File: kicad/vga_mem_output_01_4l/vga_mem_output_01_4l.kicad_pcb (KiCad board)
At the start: 4 copper layers, 80.4 x 110.6 mm, 61 parts, among them J1 Conn_01x03_Socket, J2 Conn_01x02_Socket, J3 Conn_01x08_Socket, J4 DE15_Socket_HighDensity_Mount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, J6 Conn_01x18_Socket, U1 74LS08, U10 74HCT574, U11 74HC245, U12 74AHC1GU04, U13 74LS163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

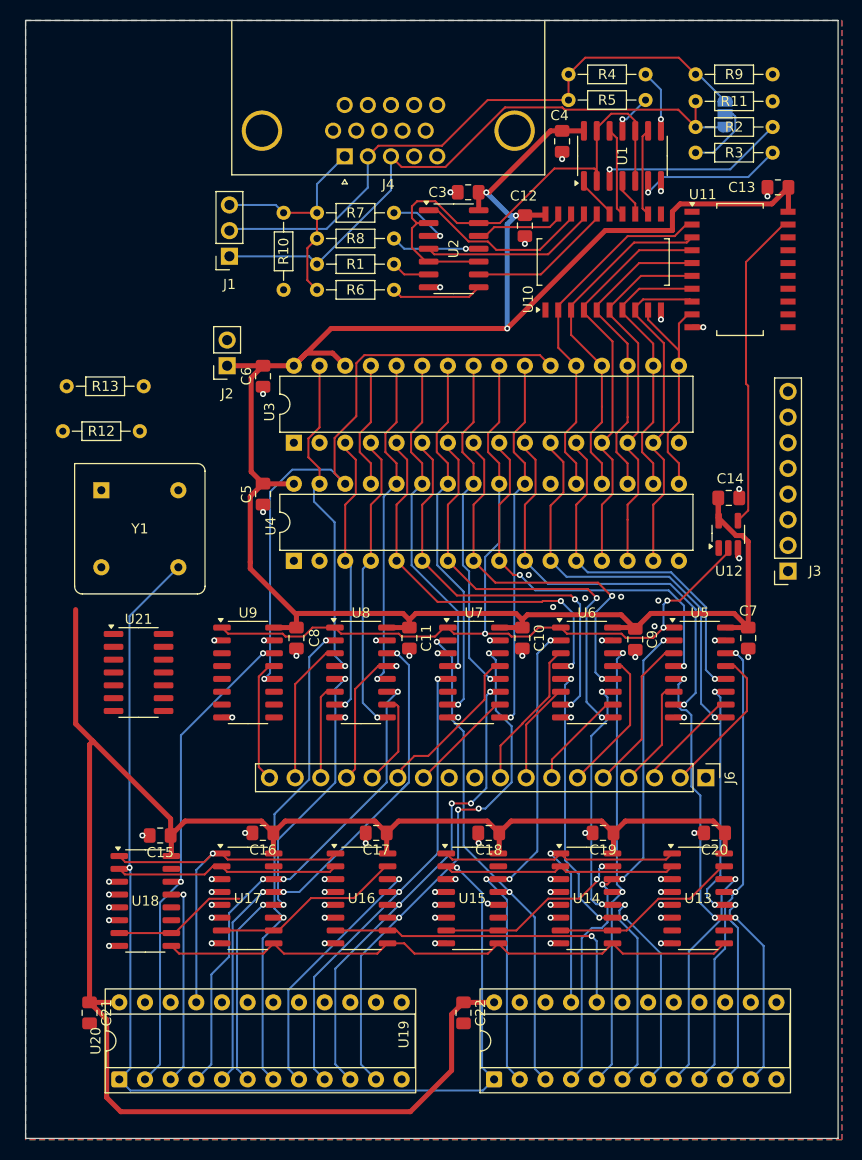
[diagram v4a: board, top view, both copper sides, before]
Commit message: finished vga rework
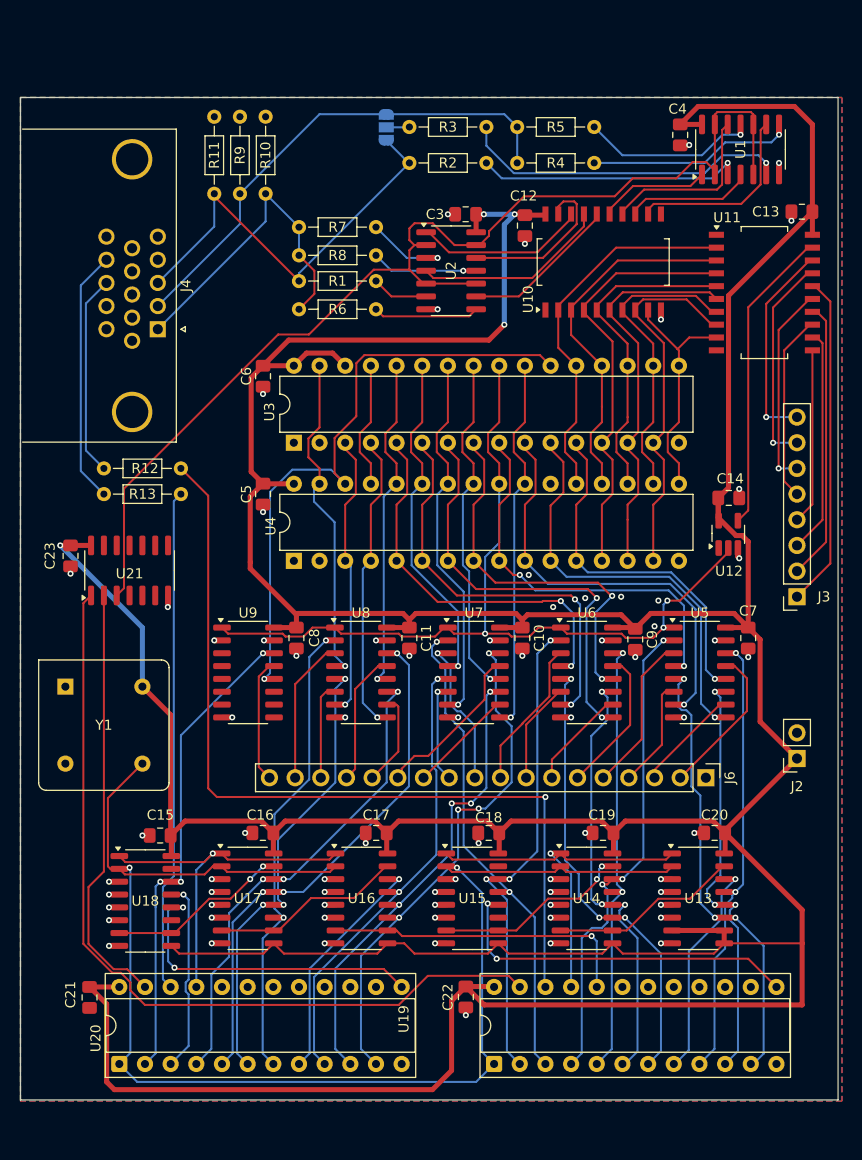
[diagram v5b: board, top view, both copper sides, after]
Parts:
- removed J1: Conn_01x03_Socket, Connector_PinSocket_2.54mm:PinSocket_1x03_P2.54mm_Vertical
- added C23: 100nF, Capacitor_SMD:C_0805_2012Metric_Pad1.18x1.45mm_HandSolder, F.Cu at (55.1, 89.9)
- moved J2 68.5 mm to (127.0, 110.0)
- moved R11 55.3 mm to (69.3, 46.5), turned to -90 degrees
- moved R9 52.9 mm to (71.9, 46.5), turned to -90 degrees
- moved JP1 33.6 mm to (86.4, 47.5)
- moved R2 28.5 mm to (96.3, 51.1)
- moved R3 28.4 mm to (96.3, 47.5)
- moved J4 25.2 mm to (63.8, 67.5), turned to -90 degrees
- moved Y1 19.8 mm to (54.6, 102.9)
- moved R10 17.2 mm to (74.4, 46.5), turned to -90 degrees
- moved U1 11.7 mm to (121.4, 49.7)
- moved C4 11.7 mm to (115.4, 48.3)
- moved R13 11.3 mm to (58.4, 83.8)
- moved U21 10.1 mm to (61.0, 91.4), turned to 90 degrees
- moved R4 10.1 mm to (106.9, 51.1)
- moved R5 5.74 mm to (106.9, 47.5)
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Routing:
- net VCC: track 457.2 -> 545.0 mm, vias 3 -> 4
- net /display_generator/H_SYNC: track 0.00 -> 85.4 mm, vias 0 -> 1
- net /display_generator/H_VA: track 0.00 -> 82.6 mm
- net /display_generator/VA_EN: track 51.4 -> 112.5 mm
- net /display_generator/V_SYNC: track 0.00 -> 49.8 mm
- net /display_generator/V_VA: track 0.00 -> 42.5 mm
- net /display_generator/H10: track 1.05 -> 35.7 mm, vias 1 -> 2
- net /CPU_D0: track 0.00 -> 33.0 mm
- net /display_generator/V10: track 0.00 -> 32.1 mm, vias 0 -> 2
- net /CPU_D1: track 0.00 -> 27.7 mm
- net Net-(J4-Pad14): track 0.00 -> 25.2 mm
- net /CPU_D2: track 0.00 -> 22.3 mm
- net /display_generator/CLOCK: track 161.5 -> 140.1 mm
- net /CPU_D6: track 0.00 -> 21.0 mm, vias 0 -> 1
- net /CPU_D7: track 0.00 -> 20.6 mm, vias 0 -> 1
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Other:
- board size 80.4 x 110.6 mm -> 80.9 x 99.2 mm

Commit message: routing fixes
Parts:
- added J1: Conn_01x03_Socket, Connector_PinSocket_2.54mm:PinSocket_1x03_P2.54mm_Vertical, F.Cu at (127.0, 103.4)
- added JP2: SolderJumper_3_Open, Jumper:SolderJumper-3_P1.3mm_Open_RoundedPad1.0x1.5mm, B.Cu at (123.7, 85.9)
- moved R10 19.1 mm to (75.2, 65.5), turned to 180 degrees
- moved R9 16.6 mm to (75.2, 62.7), turned to 180 degrees
- moved R11 14.7 mm to (75.2, 59.9), turned to 180 degrees
- moved Y1 7.62 mm to (54.6, 110.5), turned to 0 degrees
- moved R7 0.25 mm to (85.3, 57.1)
- moved R8 0.25 mm to (85.3, 59.9)
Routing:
- net /~{WE}: track 12.6 -> 68.7 mm
- net /~{PD_L}: track 0.00 -> 39.0 mm, vias 0 -> 1
- net /display_generator/H0: track 22.0 -> 57.6 mm, vias 1 -> 3
- net /H0_EXT: track 0.00 -> 15.5 mm
- net VCC: track 545.0 -> 560.5 mm, vias 4 -> 3
- net /~{A_FRONT}: track 87.0 -> 101.8 mm
- net /vga output/R_OUT: track 31.9 -> 24.8 mm
- net /display_generator/CLOCK: track 140.1 -> 145.5 mm
- net GND: track 63.0 -> 67.4 mm, vias 72 -> 94
- net /vga output/B_OUT: track 42.7 -> 38.6 mm
- net /display_generator/V10: track 32.1 -> 29.9 mm
- net /display_generator/H10: track 35.7 -> 33.8 mm
- net /A16: track 61.9 -> 60.9 mm
- net Net-(J4-Pad13): track 19.9 -> 19.1 mm
- net /vga output/G_OUT: track 49.3 -> 50.0 mm
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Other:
- board size 80.9 x 99.2 mm -> 80.9 x 100.6 mm

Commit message: switch to VCC pour on signal layers, revised signal / ref assignments
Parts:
- added C1: 100nF, Capacitor_SMD:C_0805_2012Metric_Pad1.18x1.45mm_HandSolder, F.Cu at (55.3, 99.1)
- J1: footprint Connector_PinSocket_2.54mm:PinSocket_1x03_P2.54mm_Vertical -> Connector_PinSocket_2.54mm:PinSocket_1x04_P2.54mm_Vertical
- J3: footprint Connector_PinSocket_2.54mm:PinSocket_1x08_P2.54mm_Vertical -> Connector_PinSocket_2.54mm:PinSocket_1x09_P2.54mm_Vertical
- J6: footprint Connector_PinHeader_2.54mm:PinHeader_1x18_P2.54mm_Vertical -> Connector_PinHeader_2.54mm:PinHeader_1x19_P2.54mm_Vertical
- moved J2 8.38 mm to (127.0, 118.4)
- moved J1 7.87 mm to (127.0, 111.3)
- moved J3 2.54 mm to (127.0, 96.5)
- moved C15 0.27 mm to (64.1, 117.3)
- moved U18 0.25 mm to (62.5, 123.8)
- moved C12 0.08 mm to (100.1, 57.2)
- moved C19 0.08 mm to (107.7, 117.3)
- moved C17 0.06 mm to (85.4, 117.3)
- moved C18 0.05 mm to (96.4, 117.3)
- moved C20 0.05 mm to (118.8, 117.3)
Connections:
- J1 pad 1: /~{A_FRONT} -> GND
- J1 pad 2: /~{WE} -> /~{A_FRONT}
- J1 pad 3: /H0_EXT -> /~{WE}
- J2 pad 1: VCC -> GND
- J2 pad 2: GND -> VCC
- J3 pad 1: /CPU_D0 -> GND
- J3 pad 2: /CPU_D1 -> /CPU_D0
- J3 pad 3: /CPU_D2 -> /CPU_D1
- J3 pad 4: /CPU_D3 -> /CPU_D2
- J3 pad 5: /CPU_D4 -> /CPU_D3
- J3 pad 6: /CPU_D5 -> /CPU_D4
- J3 pad 7: /CPU_D6 -> /CPU_D5
- J3 pad 8: /CPU_D7 -> /CPU_D6
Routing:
- net VCC: track 560.5 -> 424.5 mm, vias 3 -> 22
- net /~{A_FRONT}: track 101.8 -> 117.2 mm, vias 3 -> 2
- net /H0_EXT: track 15.5 -> 20.9 mm
- net /~{WE}: track 68.7 -> 73.9 mm
- net GND: track 67.4 -> 70.7 mm, vias 94 -> 117
- net /display_generator/V3: track 52.1 -> 49.5 mm, vias 4 -> 2
- net /display_generator/VA_EN: track 112.9 -> 110.5 mm, vias 0 -> 5
- net /display_generator/V0: track 23.5 -> 25.9 mm
- net Net-(R7-Pad1): track 8.60 -> 6.32 mm, vias 1 -> 0
- net /A5: track 42.8 -> 41.3 mm
- net /A4: track 38.0 -> 36.5 mm
- net /PDB_4: track 17.4 -> 18.8 mm
- net /A16: track 60.9 -> 62.3 mm
- net /display_generator/V2: track 47.0 -> 48.4 mm, vias 4 -> 2
- net /display_generator/V_VA: track 42.5 -> 41.3 mm
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- added copper zone on B.Cu, net VCC
- added copper zone on F.Cu, net VCC
- removed copper zone on B.Cu, net GND
- removed copper zone on F.Cu, net GND
